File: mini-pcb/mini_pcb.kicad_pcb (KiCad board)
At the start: 2 copper layers, 58.5 x 60.5 mm, 47 parts, among them J1 Screw_Terminal_01x02, J3 Barrel_Jack_Switch, J4 AUDIO_IN_TRS, J5 AUDIO_OUT_TRS, U1 LM1117DT-5.0, U2 OPA1664D, U3 OPA1655DBV

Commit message: ordered pcb
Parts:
- removed C11, C7: 0.1uf, Capacitor_SMD:C_0805_2012Metric
- removed R10, R11, R12: 1M, Resistor_SMD:R_0603_1608Metric
- removed R15, R17, R20: 10k, Resistor_SMD:R_0603_1608Metric
- removed R16, R18, R19, R8: 39k, Resistor_SMD:R_0603_1608Metric
- removed R23, R24: 100k, Resistor_SMD:R_0603_1608Metric
- removed U3: OPA1655DBV, Package_TO_SOT_SMD:SOT-23-5
- added 5V1: TestPoint, TestPoint:TestPoint_Pad_D2.0mm, B.Cu at (162.3, 153.2)
- added 9V1: TestPoint, TestPoint:TestPoint_Pad_D2.0mm, B.Cu at (159.0, 153.2)
- added AUDIO_IN1: TestPoint, TestPoint:TestPoint_Pad_D2.0mm, F.Cu at (160.5, 135.5)
- added AUDIO_RAW1: TestPoint, TestPoint:TestPoint_Pad_D2.0mm, F.Cu at (133.2, 116.8)
- added C13: 1nf, Capacitor_SMD:C_0805_2012Metric, F.Cu at (145.2, 126.0)
- added C14: 10uf, Capacitor_SMD:C_0805_2012Metric, F.Cu at (137.8, 117.5)
- added C15: 10uf, Capacitor_SMD:C_0805_2012Metric, F.Cu at (137.8, 123.0)
- added C16: 1nf, Capacitor_SMD:C_0805_2012Metric, F.Cu at (155.5, 124.0)
- added C17: 1nf, Capacitor_SMD:C_0805_2012Metric, F.Cu at (155.5, 118.5)
- added C18: 1uf, Capacitor_SMD:C_0805_2012Metric, F.Cu at (121.5, 120.2)
- added C19: 1uf, Capacitor_SMD:C_0805_2012Metric, F.Cu at (128.0, 120.2)
- added D2: LED, LED_SMD:LED_0805_2012Metric, F.Cu at (141.5, 164.5)
- added GND1: TestPoint, TestPoint:TestPoint_Pad_D2.0mm, B.Cu at (165.5, 153.2)
- added GND2: TestPoint, TestPoint:TestPoint_Pad_D2.0mm, F.Cu at (122.8, 144.2)
- added R27: 330, Resistor_SMD:R_0603_1608Metric, F.Cu at (141.5, 161.2)
- added U4: LP5907MFX-2.5, Package_TO_SOT_SMD:SOT-23-5, F.Cu at (124.8, 120.2)
- C1, C4: value 10UF -> 10uf; footprint Capacitor_SMD:C_0805_2012Metric -> Capacitor_Tantalum_SMD:CP_EIA-3216-18_Kemet-A
- C10: value 10uf -> 0.1uf
- C2: value 10uf -> 1nf
- R2, R9: value 1M -> 7.5k
- R25, R26: value 1k -> 100
- R3, R4, R6, R7: value 1M -> 100
- R5: value 10k -> 1M
- moved C10 56.6 mm to (123.5, 166.5), turned to 180 degrees
- moved R3 38.3 mm to (136.0, 117.5)
- moved R4 36.9 mm to (136.0, 123.0)
- moved R6 19.0 mm to (152.8, 130.2), turned to 180 degrees
- moved C3 18.0 mm to (149.0, 128.5), turned to 180 degrees
- moved C5 17.6 mm to (152.5, 128.5), turned to 180 degrees
- moved R7 16.1 mm to (149.0, 130.2)
- moved C6 15.7 mm to (155.5, 122.0)
- moved R2 13.9 mm to (152.2, 123.0), turned to 0 degrees
- moved R9 13.9 mm to (152.2, 117.5), turned to 0 degrees
- moved R5 12.7 mm to (139.5, 123.0), turned to 90 degrees
- moved C12 11.5 mm to (139.8, 120.2), turned to 180 degrees
- moved C2 11.3 mm to (145.2, 113.0), turned to 180 degrees
- moved C4 7.11 mm to (123.0, 164.2), turned to 180 degrees
- moved C9 5.47 mm to (155.5, 116.5)
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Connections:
- C1 pad 1: +5V -> +9V
- C10 pad 1: Net-(U2D--) -> +5V
- C10 pad 2: Net-(C10-Pad2) -> GND
- C2 pad 1: Net-(C2-Pad1) -> GND
- C2 pad 2: Net-(U2B-+) -> Net-(U2A--)
- C3 pad 1: AUDIO_OUT_JACK_RIGHT_BUF -> Net-(C3-Pad1)
- C3 pad 2: Net-(C3-Pad2) -> Net-(U2D-+)
- C4 pad 1: +9V -> +5V
- C5 pad 1: AUDIO_OUT_JACK_LEFT_BUF -> Net-(C5-Pad1)
- C5 pad 2: Net-(C5-Pad2) -> Net-(U2C-+)
- C6 pad 2: Net-(U2A-+) -> Net-(C6-Pad2)
- C9 pad 1: Net-(U2C--) -> Net-(C17-Pad2)
- R13 pad 1: Net-(R13-Pad1) -> Net-(U2A--)
- R14 pad 1: Net-(R14-Pad1) -> Net-(U2B--)
- R2 pad 1: GND -> Net-(U2C--)
- R25 pad 1: Net-(C10-Pad2) -> Net-(C9-Pad2)
- R26 pad 1: Net-(C9-Pad2) -> Net-(C6-Pad2)
- R3 pad 1: GND -> Net-(C14-Pad1)
- R3 pad 2: Net-(C5-Pad2) -> AUDIO_IN_JACK_LEFT
- R4 pad 1: Net-(C5-Pad2) -> Net-(C15-Pad1)
- R4 pad 2: +5V -> AUDIO_IN_JACK_RIGHT
- R5 pad 1: Net-(U2C-+) -> Net-(U2B-+)
- R5 pad 2: GND -> +2.5V
- R6 pad 1: Net-(U3-+) -> AUDIO_OUT_JACK_LEFT_BUF
- R6 pad 2: +5V -> Net-(C5-Pad1)
- R7 pad 1: GND -> AUDIO_OUT_JACK_RIGHT_BUF
- R7 pad 2: Net-(U3-+) -> Net-(C3-Pad1)
- R9 pad 1: GND -> Net-(U2D--)
- R9 pad 2: Net-(C2-Pad1) -> Net-(C17-Pad2)
- U2 pad 1: Net-(R13-Pad1) -> Net-(U2A--)
- U2 pad 7: Net-(R14-Pad1) -> Net-(U2B--)
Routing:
- net +5V: track 133.0 -> 39.4 mm, vias 3 -> 10
- net Net-(C5-Pad2): track 26.4 -> 0.00 mm
- net +9V: track 30.6 -> 56.0 mm, vias 0 -> 1
- net Net-(C3-Pad2): track 22.3 -> 0.00 mm
- net Net-(C2-Pad1): track 18.4 -> 0.00 mm
- net AUDIO_OUT_JACK_RIGHT_BUF: track 2.49 -> 16.8 mm
- net AUDIO_OUT_JACK_LEFT_BUF: track 2.54 -> 15.6 mm
- net AUDIO_IN_JACK_RIGHT: track 2.85 -> 15.1 mm
- net +2.5V: track 13.7 -> 22.0 mm, vias 0 -> 3
- net Net-(R13-Pad1): track 5.19 -> 0.00 mm
- net AUDIO_IN_JACK_LEFT: track 3.54 -> 8.15 mm
- net Net-(R14-Pad1): track 4.26 -> 0.00 mm
- net Net-(C17-Pad2): track 0.00 -> 3.78 mm
- net Net-(U3-+): track 3.08 -> 0.00 mm
- net Net-(U2D-+): track 14.3 -> 11.3 mm
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- added copper zone on F.Cu, net +5V
- added copper zone on In2.Cu, net +5V
- added copper zone on In1.Cu, net GND
- added copper zone on F.Cu, net POWER_JACK_PWR
- removed copper zone on B.Cu, net GND
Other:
- copper layers 2 -> 4

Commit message: made mini-pcb report
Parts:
- removed C18, C19: 1uf, Capacitor_SMD:C_0805_2012Metric
- removed U4: LP5907MFX-2.5, Package_TO_SOT_SMD:SOT-23-5
- added R10: 2M, Resistor_SMD:R_0603_1608Metric, F.Cu at (141.0, 116.8)
- added R8: 2M, Resistor_SMD:R_0603_1608Metric, F.Cu at (139.5, 123.8)
- C14, C15: value 10uf -> 47nF
- R1, R5: value 1M -> 2M
- moved R5 1.68 mm to (141.0, 123.8)
- moved R1 0.70 mm to (139.5, 116.8)
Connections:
- R1 pad 2: +2.5V -> +5V
- R5 pad 2: +2.5V -> +5V
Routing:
- net +2.5V: track 22.0 -> 0.00 mm, vias 3 -> 0
- net +5V: track 39.4 -> 34.7 mm, vias 10 -> 11
- net GND: track 22.4 -> 21.0 mm, vias 30 -> 29

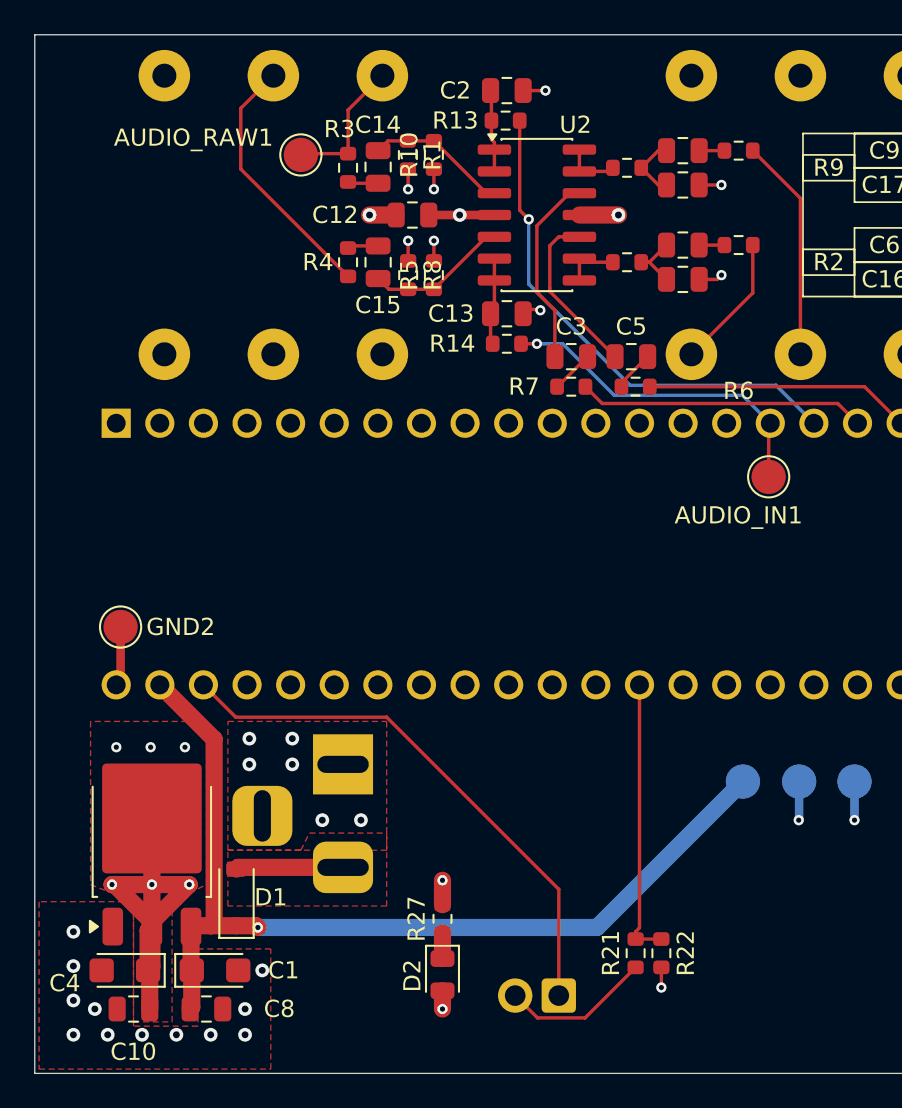
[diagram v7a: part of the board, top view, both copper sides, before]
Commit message: I will be re writing the code to use the daisy-embassy library because the Daisy one i have been using has a strange but crush effect when there is just a normal passthrough but the daisy-embassy example works well with my PCB also there was a testing problem earlyer with the PCB and the PCB works fine with no changes
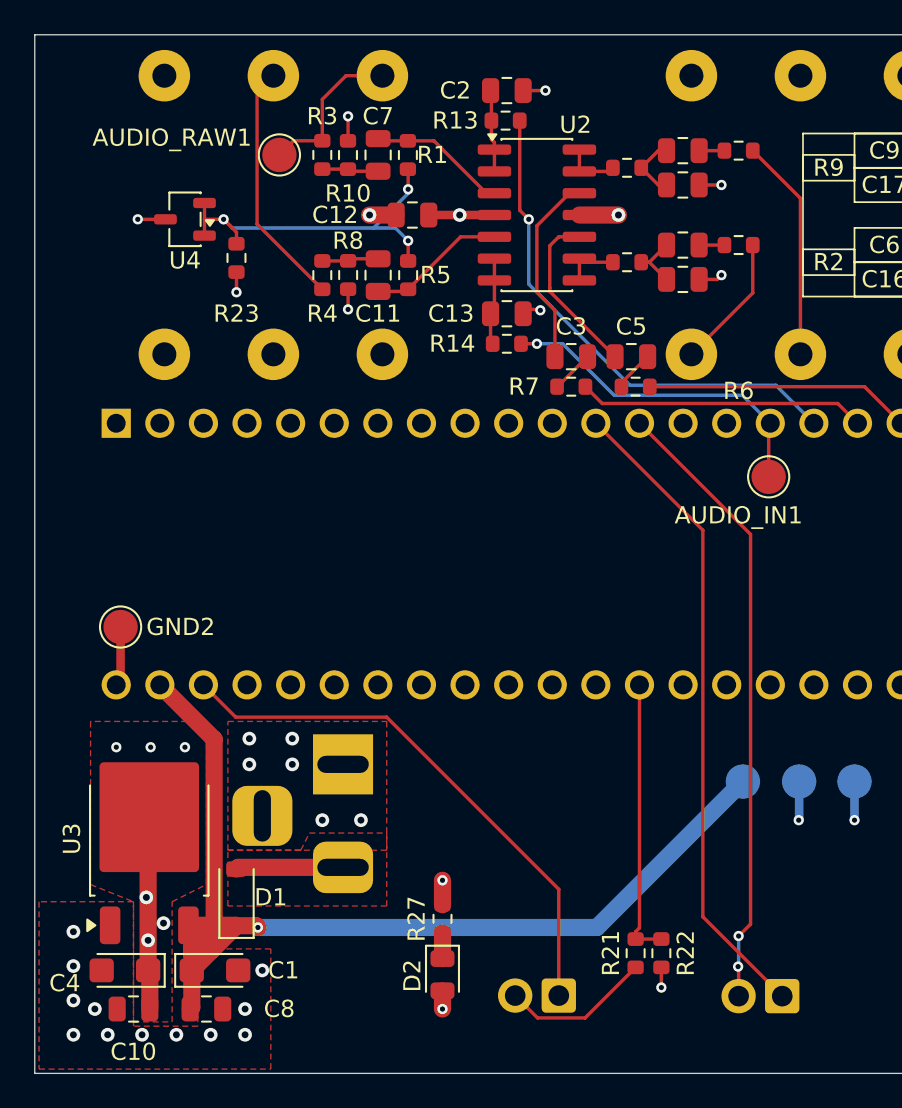
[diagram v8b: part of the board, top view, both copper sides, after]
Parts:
- removed C14, C15: 47nF, Capacitor_SMD:C_0805_2012Metric
- removed U1: LM1117DT-5.0, Package_TO_SOT_SMD:TO-252-3_TabPin2
- added C11: 10uf, Capacitor_SMD:C_0805_2012Metric, F.Cu at (137.8, 123.8)
- added C7: 10uf, Capacitor_SMD:C_0805_2012Metric, F.Cu at (137.8, 116.8)
- added J6: Screw_Terminal_01x02, TerminalBlock:TerminalBlock_Xinya_XY308-2.54-2P_1x02_P2.54mm_Horizontal, B.Cu at (161.3, 165.8)
- added R23: 1k, Resistor_SMD:R_0603_1608Metric, F.Cu at (129.5, 122.8)
- added U3: LM1117DT-5.0, Package_TO_SOT_SMD:TO-252-2, F.Cu at (124.4, 156.6)
- added U4: CJ431, Package_TO_SOT_SMD:SOT-23-3, F.Cu at (126.5, 120.5)
- moved R10 5.01 mm to (136.0, 116.8), turned to -90 degrees
- moved R8 3.50 mm to (136.0, 123.7), turned to 90 degrees
- moved R3 1.68 mm to (134.5, 116.8)
- moved R4 1.68 mm to (134.5, 123.8)
- moved R5 1.50 mm to (139.5, 123.8)
- moved AUDIO_RAW1 1.25 mm to (132.0, 116.8)
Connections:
- A1 pad 12: unconnected-(A1-I2C1_SCL-Pad12) -> Net-(A1-I2C1_SCL)
- A1 pad 13: unconnected-(A1-I2C1_SDA-Pad13) -> Net-(A1-I2C1_SDA)
- R1 pad 2: +5V -> +2.5V
- R10 pad 2: Net-(U2A-+) -> Net-(C7-Pad1)
- R3 pad 1: Net-(C14-Pad1) -> Net-(C7-Pad1)
- R4 pad 1: Net-(C15-Pad1) -> Net-(C11-Pad1)
- R5 pad 2: +5V -> +2.5V
- R8 pad 2: Net-(U2B-+) -> Net-(C11-Pad1)
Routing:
- net Net-(A1-I2C1_SCL): track 0.00 -> 37.9 mm
- net Net-(A1-I2C1_SDA): track 0.00 -> 36.4 mm, vias 0 -> 2
- net +2.5V: track 0.00 -> 21.4 mm, vias 0 -> 3
- net +5V: track 34.7 -> 19.6 mm, vias 11 -> 10
- net +9V: track 56.0 -> 64.2 mm
- net Net-(C11-Pad1): track 0.00 -> 3.32 mm
- net Net-(C7-Pad1): track 0.00 -> 3.30 mm
- net Net-(C15-Pad1): track 2.00 -> 0.00 mm
- net Net-(C14-Pad1): track 2.00 -> 0.00 mm
- net GND: track 21.0 -> 22.9 mm, vias 29 -> 30
- net AUDIO_IN_JACK_LEFT: track 8.15 -> 9.32 mm
- net AUDIO_IN_JACK_RIGHT: track 15.1 -> 14.4 mm
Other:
- board text added: "SCL"
- board text added: "SDA"
